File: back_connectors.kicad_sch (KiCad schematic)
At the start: 78 parts, among them J10 DB25_Male_MountingHoles, J11 DB25_Male_MountingHoles, J12 DB25_Male_MountingHoles, J13 DB25_Male_MountingHoles, J14 goldpins, J6 IDC10, J7 Lichtenprog_conn, J8 IDC10, J9 IDC10, U10 74HC244, U5 PCA9555PW, U6 PCA9555PW, U7 74HC244, U8 74HC244, U9 PCA9555PW

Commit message: routing mostly done, fixing schematic issues
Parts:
- removed J14: goldpins, Connector_PinHeader_2.54mm:PinHeader_1x10_P2.54mm_Vertical, symbol Connector_Generic:Conn_01x10
- removed TP8, TP9: RLPAD, TestPoint:TestPoint_Pad_D1.0mm, symbol Connector:TestPoint
- added F1, F10, F11, F12, F13, F14, F15, F16, F2, F3, F4, F5, F6, F7, F8, F9: FUSE_1206, Fuse:Fuse_1206_3216Metric, symbol Device:Fuse
- added J14: Proto_matrix_14x10, Critbit_lib:Proto_matrix_14x10, symbol Critbit_lib:Proto_matrix_14x10
- added JP8: IOEX_A2_SEL, Jumper:SolderJumper-3_P2.0mm_Open_TrianglePad1.0x1.5mm, symbol Jumper:SolderJumper_3_Open
- H10, H7, H8, H9: value SCRHOLE -> HOLE_B2
- R21, R22, R23, R24, R25, R26, R27, R29, R30, R31, R32, R33: value 10k -> 10k_1206
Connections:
- net +5VD: now also JP8.3 (B)
- net B2_OUT_BUF_ENA: now also R35.2, U8.1 (1OE), U8.19 (2OE)
- net GND: now also J14.A1, J14.J1
- net GND2: now also JP8.1 (A)
- net INPUT_10: now also U10.5 (2Y1); no longer U10.16 (1Y1)
- net INPUT_11: now also U10.7 (2Y2); no longer U10.14 (1Y2)
- net INPUT_12: now also U10.9 (2Y3); no longer U10.12 (1Y3)
- net INPUT_9: now also U10.3 (2Y0); no longer U10.18 (1Y0)
- net OUT_BUFF_ENA: no longer R35.2, U8.1 (1OE), U8.19 (2OE)
- net SINK1: now also F1.1; no longer J11.23 (P23)
- net SINK10: now also F10.1; no longer J11.5
- net SINK11: now also F11.1; no longer J11.17 (P17)
- net SINK12: now also F12.1; no longer J11.4
- net SINK13: now also F13.1; no longer J11.3
- net SINK14: now also F14.1; no longer J11.15 (P15)
- net SINK15: now also F15.1; no longer J11.2
- net SINK16: now also F16.1; no longer J11.14 (P14)
- net SINK2: now also F2.1; no longer J11.10
- net SINK3: now also F3.1; no longer J11.22 (P22)
- net SINK4: now also F4.1; no longer J11.9
- net SINK5: now also F5.1; no longer J11.8
- net SINK6: now also F6.1; no longer J11.20 (P20)
- net SINK7: now also F7.1; no longer J11.7
- net SINK8: now also F8.1; no longer J11.19 (P19)
- net SINK9: now also F9.1; no longer J11.18 (P18)
- net at J13.9, R27.1: no longer C28.1
- net at R27.2, U7.13 (2A2): now also C28.1
- net at J13.25 (P25), R21.1: no longer C22.1
- net at R21.2, U7.2 (1A0): now also C22.1
- net at J13.6, R33.1: no longer C33.1
- net at R29.2, U7.11 (2A3): now also C29.1
- net at R26.2, U7.15 (2A1): now also C27.1
- net at R25.2, U7.17 (2A0): now also C26.1
- net at R22.2, U7.4 (1A1): now also C23.1
- net at R23.2, U7.6 (1A2): now also C24.1
- net at R24.2, U7.8 (1A3): now also C25.1
- net at J13.19 (P19), R32.1: no longer C32.1
- net at J13.10, R25.1: no longer C26.1
- net at J13.7, R31.1: no longer C31.1
- net at R31.2: now also C31.1, U10.15 (2A1); no longer U10.4 (1A1)
- net at J13.11, R24.1: no longer C25.1
- net at U6.3 (A2): now also U9.3 (A2), JP8.2 (C)
- net at J13.12, R22.1: no longer C23.1
- net at R30.2: now also C30.1, U10.17 (2A0); no longer U10.2 (1A0)
- net at R32.2: now also C32.1, U10.13 (2A2); no longer U10.6 (1A2)
- net at R33.2: now also C33.1, U10.11 (2A3); no longer U10.8 (1A3)
- net at J13.20 (P20), R30.1: no longer C30.1
- net at J13.21 (P21), R29.1: no longer C29.1
- net at J13.22 (P22), R26.1: no longer C27.1
- net at J6.10 (Pin_10), J7.7 (GND): now also J6.7 (Pin_7), J6.8 (Pin_8), J7.6 (GND)
- net at J13.14 (P14): now also J14.I1
- net at J13.15 (P15): now also J14.G1
- net at J13.16 (P16): now also J14.E1
- net at J13.17 (P17): now also J14.C1
- net at J13.2: now also J14.H1
- net at J13.24 (P24), R23.1: no longer C24.1
- net at J13.3: now also J14.F1
- net at J13.4: now also J14.D1
- net at J13.5: now also J14.B1
- new net: F5.2, J11.8
- new net: F16.2, J11.14 (P14)
- new net: F6.2, J11.20 (P20)
- new net: F8.2, J11.19 (P19)
- new net: F11.2, J11.17 (P17)
- new net: F4.2, J11.9
- new net: F12.2, J11.4
- new net: R36.2, U10.2 (1A0), U10.4 (1A1), U10.6 (1A2), U10.8 (1A3)
- new net: F13.2, J11.3
- new net: F10.2, J11.5
- new net: F9.2, J11.18 (P18)
- new net: F2.2, J11.10
- new net: F14.2, J11.15 (P15)
- new net: F3.2, J11.22 (P22)
- new net: F15.2, J11.2
- new net: F1.2, J11.23 (P23)
- new net: F7.2, J11.7
- no-connect marks 10 -> 44
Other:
- sheet Relay1 ports: added VCOIL; removed none
- sheet Relay10 ports: added VCOIL; removed none
- sheet Relay11 ports: added VCOIL; removed none
- sheet Relay12 ports: added VCOIL; removed none
- sheet Relay13 ports: added VCOIL; removed none
- sheet Relay14 ports: added VCOIL; removed none
- sheet Relay15 ports: added VCOIL; removed none
- sheet Relay2 ports: added VCOIL; removed none
- sheet Relay3 ports: added VCOIL; removed none
- sheet Relay4 ports: added VCOIL; removed none
- sheet Relay5 ports: added VCOIL; removed none
- sheet Relay6 ports: added VCOIL; removed none
- sheet Relay7 ports: added VCOIL; removed none
- sheet Relay8 ports: added VCOIL; removed none
- sheet Relay9 ports: added VCOIL; removed none
- note added: "12 inputs + 8 GPIO to protoboard area"
- note added: "15 relays"
- note added: "16 NMOS switches"
- note added: "8 optocouplers + 8 5V outputs"
- note added: "Fuse from JLC: C183160"
- note removed: "16 relays onboard"
- note removed: "Fuse example: C183160"
- moved on the sheet: C15, C16, C17, C18, C19, C20, C21, C22, C23, C24, C25, C26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

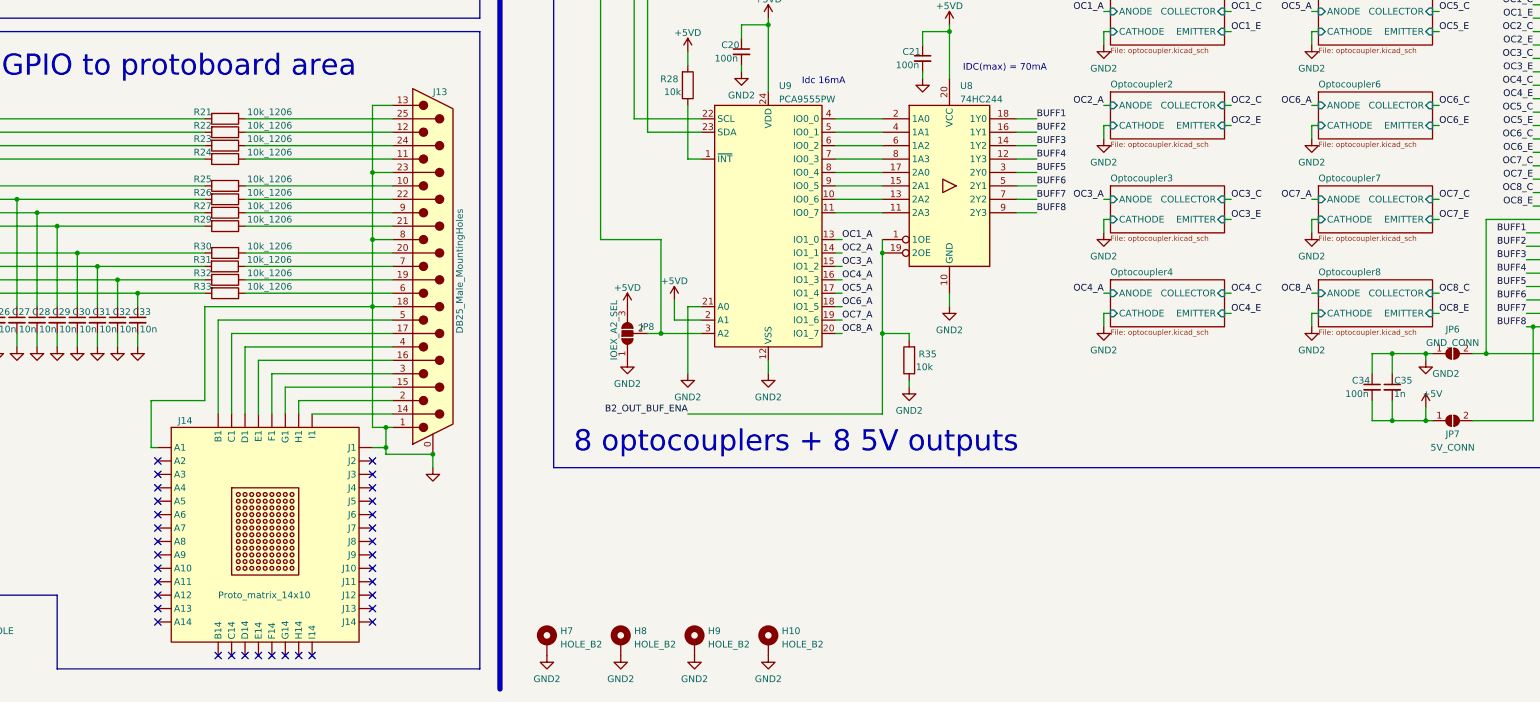
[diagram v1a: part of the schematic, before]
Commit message: finish routing and silk
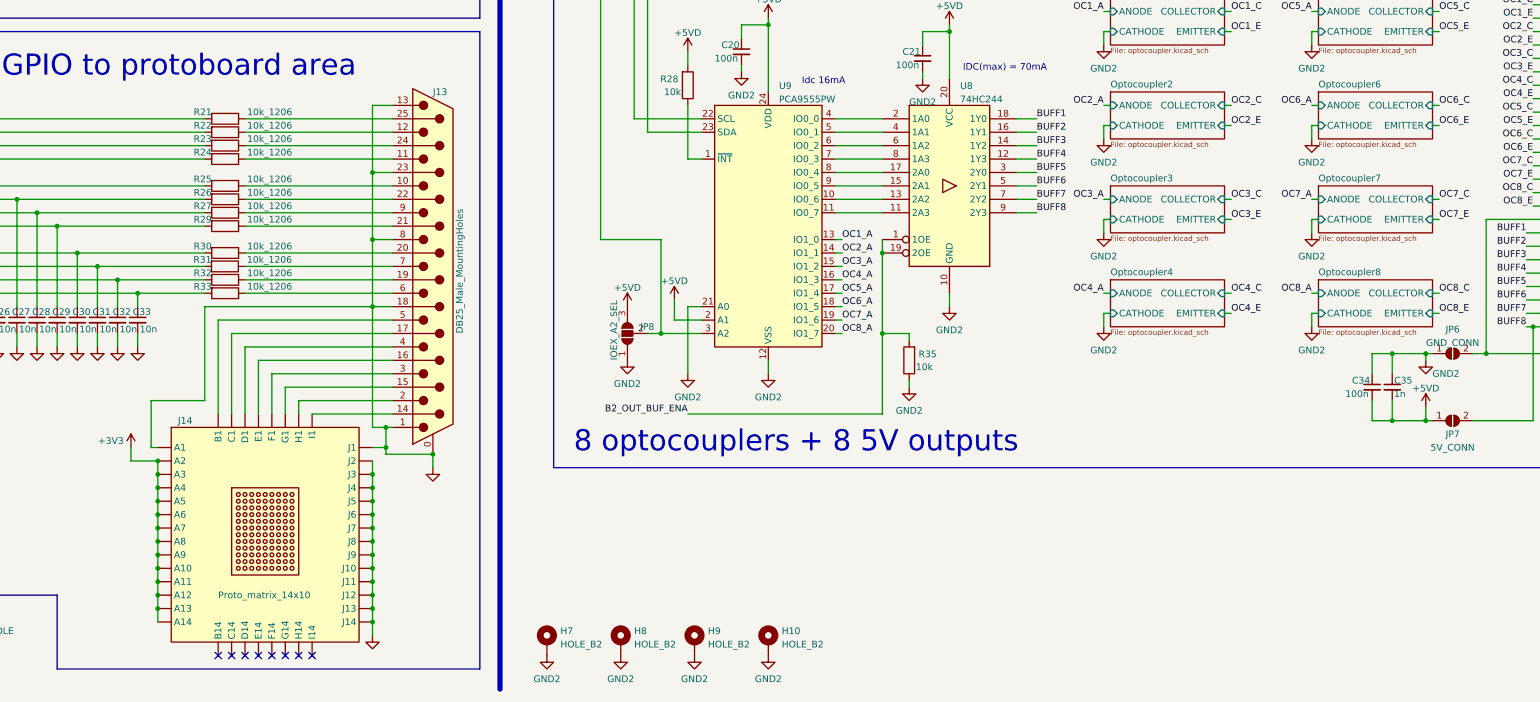
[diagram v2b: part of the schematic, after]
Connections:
- net +3V3: now also J14.A10, J14.A11, J14.A12, J14.A13, J14.A14, J14.A2, J14.A3, J14.A4, J14.A5, J14.A6, J14.A7, J14.A8, J14.A9
- net +5V: no longer C34.2, C35.2, JP7.1 (A)
- net +5VD: now also C34.2, C35.2, JP7.1 (A)
- net GND: now also J14.J10, J14.J11, J14.J12, J14.J13, J14.J14, J14.J2, J14.J3, J14.J4, J14.J5, J14.J6, J14.J7, J14.J8, J14.J9; no longer C21.2
- net GND2: now also C21.2
- no-connect marks 44 -> 18

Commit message: prod files
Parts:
- added C56: 220u, Capacitor_THT:CP_Radial_D8.0mm_P3.50mm, symbol Device:C_Polarized
- R21, R22, R23, R24, R25, R26, R27, R29, R30, R31, R32, R33: footprint Resistor_SMD:R_0402_1005Metric -> Resistor_SMD:R_1206_3216Metric_Pad1.30x1.75mm_HandSolder
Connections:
- net +5VD: now also C56.1
- net B2_OUT_BUF_ENA: now also J9.8 (Pin_8); no longer J9.7 (Pin_7)
- net B2_SCL: now also J9.3 (Pin_3); no longer J9.4 (Pin_4)
- net B2_SDA: now also J9.5 (Pin_5); no longer J9.6 (Pin_6)
- net GND2: now also C56.2
- net at J6.7 (Pin_7), J6.8 (Pin_8), J7.6 (GND)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: no longer J6.10 (Pin_10)
- net at J6.9 (Pin_9), J7.8 (5V): now also J6.10 (Pin_10)
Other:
- moved on the sheet: J8

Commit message: from future import missing resistors
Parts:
- added R146, R147, R148, R149, R150, R151, R152, R153, R154, R155, R156, R157: 10k, symbol Device:R_Small
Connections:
- net +VDC: now also J11.1, J11.14 (P14), J11.2; no longer J11.12, J11.13, J11.25 (P25)
- net BUFF1: now also J12.22 (P22); no longer J12.17 (P17)
- net BUFF2: now also J12.10; no longer J12.4
- net BUFF3: now also J12.23 (P23); no longer J12.16 (P16)
- net BUFF4: now also J12.11; no longer J12.3
- net BUFF5: now also J12.24 (P24); no longer J12.15 (P15)
- net BUFF6: now also J12.12; no longer J12.2
- net BUFF7: now also J12.25 (P25); no longer J12.14 (P14)
- net BUFF8: now also J12.13; no longer J12.1
- net GND: now also J11.13, J11.15 (P15), J11.18 (P18), J11.23 (P23), J11.3, J11.8, J13.16 (P16), J13.21 (P21), J13.6, R146.2, R147.2, R148.2, R149.2, R150.2, R151.2, R152.2, R153.2, R154.2, R155.2, R156.2, R157.2; no longer J11.1, J11.11, J11.16 (P16), J11.21 (P21), J11.24 (P24), J11.6, J13.18 (P18), J13.23 (P23), J13.8
- net GND2: now also J10.0 (PAD)
- net OC1_C: now also J12.1; no longer J12.13
- net OC1_E: now also J12.14 (P14); no longer J12.25 (P25)
- net OC2_C: now also J12.2; no longer J12.12
- net OC2_E: now also J12.15 (P15); no longer J12.24 (P24)
- net OC3_C: now also J12.3; no longer J12.11
- net OC3_E: now also J12.16 (P16); no longer J12.23 (P23)
- net OC4_C: now also J12.4; no longer J12.10
- net OC4_E: now also J12.17 (P17); no longer J12.22 (P22)
- net OC5_C: now also J12.5; no longer J12.9
- net OC5_E: now also J12.18 (P18); no longer J12.21 (P21)
- net OC6_C: now also J12.6; no longer J12.8
- net OC6_E: now also J12.19 (P19); no longer J12.20 (P20)
- net OC7_E: now also J12.20 (P20); no longer J12.19 (P19)
- net OC8_C: now also J12.8; no longer J12.6
- net OC8_E: now also J12.21 (P21); no longer J12.18 (P18)
- net RL10_A: now also J10.10; no longer J10.4
- net RL10_B: now also J10.23 (P23); no longer J10.16 (P16)
- net RL11_A: now also J10.11; no longer J10.3
- net RL11_B: now also J10.24 (P24); no longer J10.15 (P15)
- net RL12_A: now also J10.12; no longer J10.2
- net RL12_B: now also J10.25 (P25); no longer J10.14 (P14)
- net RL1_A: now also J10.1; no longer J10.13
- net RL1_B: now also J10.14 (P14); no longer J10.25 (P25)
- net RL2_A: now also J10.2; no longer J10.12
- net RL2_B: now also J10.15 (P15); no longer J10.24 (P24)
- net RL3_A: now also J10.3; no longer J10.11
- net RL3_B: now also J10.16 (P16); no longer J10.23 (P23)
- net RL4_A: now also J10.4; no longer J10.10
- net RL4_B: now also J10.17 (P17); no longer J10.22 (P22)
- net RL5_A: now also J10.5; no longer J10.9
- net RL5_B: now also J10.18 (P18); no longer J10.21 (P21)
- net RL6_A: now also J10.6; no longer J10.8
- net RL6_B: now also J10.19 (P19); no longer J10.20 (P20)
- net RL7_B: now also J10.20 (P20); no longer J10.19 (P19)
- net RL8_A: now also J10.8; no longer J10.6
- net RL8_B: now also J10.21 (P21); no longer J10.18 (P18)
- net RL9_A: now also J10.9; no longer J10.5
- net RL9_B: now also J10.22 (P22); no longer J10.17 (P17)
- net at F5.2: now also J11.6; no longer J11.8
- net at F16.2: now also J11.25 (P25); no longer J11.14 (P14)
- net at J12.0 (PAD), JP6.2 (B): now also J12.9; no longer J12.5
- net at F6.2: now also J11.19 (P19); no longer J11.20 (P20)
- net at R27.1: now also J13.5; no longer J13.9
- net at C28.1, R27.2, U7.13 (2A2): now also R152.1
- net at R21.1: now also J13.14 (P14); no longer J13.25 (P25)
- net at C22.1, R21.2, U7.2 (1A0): now also R154.1
- net at C33.1, R33.2, U10.11 (2A3): now also R146.1
- net at C29.1, R29.2, U7.11 (2A3): now also R153.1
- net at C27.1, R26.2, U7.15 (2A1): now also R151.1
- net at C26.1, R25.2, U7.17 (2A0): now also R150.1
- net at C23.1, R22.2, U7.4 (1A1): now also R155.1
- net at C24.1, R23.2, U7.6 (1A2): now also R156.1
- net at C25.1, R24.2, U7.8 (1A3): now also R157.1
- net at C32.1, R32.2, U10.13 (2A2): now also R147.1
- net at R25.1: now also J13.4; no longer J13.10
- net at C31.1, R31.2, U10.15 (2A1): now also R148.1
- net at F8.2: now also J11.20 (P20); no longer J11.19 (P19)
- net at F11.2: now also J11.22 (P22); no longer J11.17 (P17)
- net at R24.1: now also J13.3; no longer J13.11
- net at F4.2: now also J11.5; no longer J11.9
- net at F12.2: now also J11.10; no longer J11.4
- net at R22.1: now also J13.2; no longer J13.12
- net at C30.1, R30.2, U10.17 (2A0): now also R149.1
- net at F13.2: now also J11.11; no longer J11.3
- net at R33.1: now also J13.8; no longer J13.6
- net at R26.1: now also J13.17 (P17); no longer J13.22 (P22)
- net at J14.I1: now also J13.25 (P25); no longer J13.14 (P14)
- net at J13.15 (P15): now also R23.1; no longer J14.G1
- net at J14.E1: now also J13.23 (P23); no longer J13.16 (P16)
- net at J14.C1: now also J13.22 (P22); no longer J13.17 (P17)
- net at J13.19 (P19): now also R30.1; no longer R32.1
- net at J14.H1: now also J13.12; no longer J13.2
- net at J13.20 (P20): now also R32.1; no longer R30.1
- net at R29.1: now also J13.18 (P18); no longer J13.21 (P21)
- net at J13.24 (P24): now also J14.G1; no longer R23.1
- net at J14.F1: now also J13.11; no longer J13.3
- net at J14.D1: now also J13.10; no longer J13.4
- net at J14.B1: now also J13.9; no longer J13.5
- net at F10.2: now also J11.9; no longer J11.5
- net at F9.2: now also J11.21 (P21); no longer J11.18 (P18)
- net at F2.2: now also J11.4; no longer J11.10
- net at F14.2: now also J11.24 (P24); no longer J11.15 (P15)
- net at F3.2: now also J11.17 (P17); no longer J11.22 (P22)
- net at F15.2: now also J11.12; no longer J11.2
- net at F1.2: now also J11.16 (P16); no longer J11.23 (P23)
- new net: J10.13, JP4.2 (B)
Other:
- note added: "Changelog: 1.0 * Initial release 1.1 * Added pulldown resistors on input [DONE] * Fixed invalid DB25 connector orientation [DONE] * fixed UART and I2C IDC10 connectors between boards [TODO]"
- moved on the sheet: C22, C23, C24, C25, C26, C27, C28, C29, C30, C31, C32, C33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
